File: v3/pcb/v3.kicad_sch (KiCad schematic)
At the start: 193 parts, among them SW1 SW_Push, SW10 SW_Push, SW11 SW_Push, SW12 SW_Push, SW13 SW_Push, SW14 SW_Push, SW15 SW_Push, SW16 SW_Push, SW17 SW_Push, SW18 SW_Push, SW19 SW_Push, SW2 SW_Push, SW20 SW_Push, SW21 SW_Push, SW22 SW_Push, SW23 SW_Push, SW24 SW_Push, SW25 SW_Push, SW26 SW_Push, SW27 SW_Push, SW28 SW_Push, SW29 SW_Push, SW3 SW_Push, SW30 SW_Push, SW31 SW_Push, SW32 SW_Push, SW33 SW_Push, SW34 SW_Push, SW35 SW_Push, SW36 SW_Push, SW37 SW_Push, SW38 SW_Push, SW39 SW_Push, SW4 SW_Push, SW40 SW_Push, SW41 SW_Push, SW42 SW_Push, SW43 SW_Push, SW44 SW_Push, SW45 SW_Push, SW46 SW_Push, SW47 SW_Push, SW48 SW_Push, SW49 SW_Push, SW5 SW_Push, SW50 SW_Push, SW51 SW_Push, SW52 SW_Push, SW53 SW_Push, SW54 SW_Push, SW55 SW_Push, SW56 SW_Push, SW57 SW_Push, SW58 SW_Push, SW59 SW_Push, SW6 SW_Push, SW60 SW_Push, SW61 SW_Push, SW62 SW_Push, SW63 SW_Push, SW64 SW_Push, SW65 SW_Push, SW66 SW_Push, SW67 SW_Push, SW68 SW_Push, SW69 SW_Push, SW7 SW_Push, SW70 SW_Push, SW71 SW_Push, SW72 SW_Push, SW73 SW_Push, SW74 SW_Push, SW75 SW_Push, SW76 SW_Push, SW77 SW_Push, SW78 SW_Push, SW79 SW_Push, SW8 SW_Push, SW80 SW_Push, SW81 SW_Push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

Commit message: Add new layout for v3
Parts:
- added D80, D90, D92: D, Diode_SMD:D_SOD-323F, symbol Device:D
- added SW80, SW90, SW92: SW_Push, Switch_Keyboard_Cherry_MX:SW_Cherry_MX_PCB_1.00u, symbol Switch:SW_Push
- renumbered D80 to D81, D81 to D82, D82 to D83, D83 to D84, D84 to D85, D85 to D86, D86 to D87, D87 to D88, D88 to D89, D89 to D91, D90 to D93, D91 to D94, D92 to D95, D93 to D96, D94 to D97, D95 to D98, D96 to D99, SW80 to SW81, SW81 to SW82, SW82 to SW83, SW83 to SW84, SW84 to SW85, SW85 to SW86, SW86 to SW87, SW87 to SW88, SW88 to SW89, SW89 to SW91, SW90 to SW93, SW91 to SW94, SW92 to SW95, SW93 to SW96, SW94 to SW97, SW95 to SW98, SW96 to SW99
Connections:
- net COL12: now also SW80.1
- net COL4: now also SW90.1
- net COL8: now also SW92.1
- net ROW4: now also D80.1 (K)
- net ROW5: now also D90.1 (K), D92.1 (K)
- new net: D80.2 (A), SW80.2
- new net: D90.2 (A), SW90.2
- new net: D92.2 (A), SW92.2

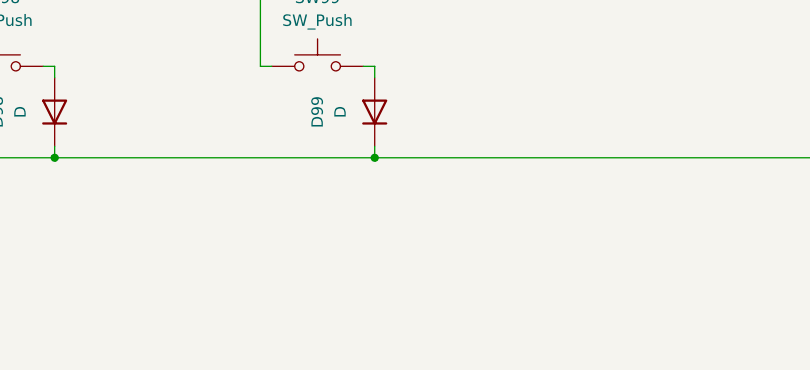
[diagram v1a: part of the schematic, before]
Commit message: Replace switch footprints with hotswap sockets
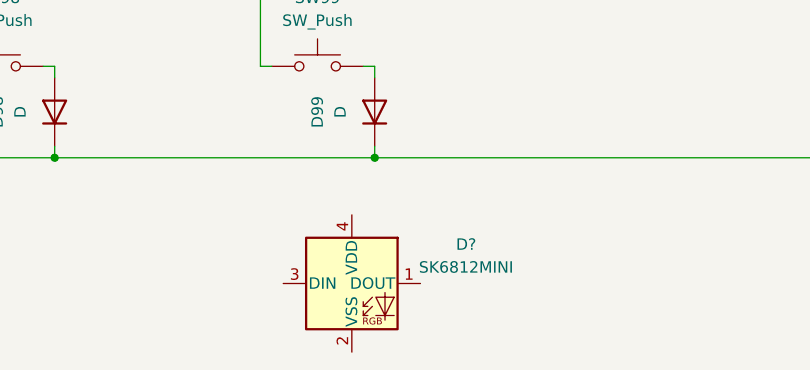
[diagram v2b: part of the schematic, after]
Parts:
- added D?: SK6812MINI, prettylib:SK6812_mini_e_flipable, symbol LED:SK6812MINI
- SW1, SW10, SW11, SW12, SW13, SW14, SW15, SW16, SW17, SW18, SW19, SW2, SW20, SW21, SW22, SW23, SW24, SW25, SW26, SW27, SW28, SW29, SW3, SW30, SW31, SW32, SW33, SW34, SW35, SW36, SW37, SW38, SW39, SW4, SW40, SW41, SW42, SW43, SW44, SW45, SW46, SW47, SW48, SW49, SW5, SW50, SW51, SW52, SW53, SW54, SW55, SW56, SW57, SW58, SW59, SW6, SW60, SW61, SW62, SW63, SW64, SW65, SW66, SW67, SW68, SW69, SW7, SW70, SW71, SW72, SW73, SW74, SW75, SW76, SW77, SW78, SW79, SW8, SW80, SW81, SW82, SW83, SW84, SW85, SW86, SW87, SW88, SW89, SW9, SW90, SW91, SW92, SW93, SW94, SW95, SW96, SW97, SW98, SW99: footprint Switch_Keyboard_Cherry_MX:SW_Cherry_MX_PCB_1.00u -> prettylib:MX_KAILH_SOCKET_1U

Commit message: Add level shifter and everything else for the RGBs
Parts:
- removed D?: SK6812MINI, prettylib:SK6812_mini_e_flipable, symbol LED:SK6812MINI
- added C1, C10, C11, C12, C13, C14, C15, C16, C17, C18, C19, C2, C20, C21, C22, C23, C24, C25, C26, C27, C28, C29, C3, C30, C31, C32, C33, C34, C35, C36, C37, C38, C39, C4, C40, C41, C42, C43, C44, C45, C46, C47, C48, C49, C5, C50, C51, C52, C53, C54, C55, C56, C57, C58, C59, C6, C60, C61, C62, C63, C64, C65, C66, C67, C68, C69, C7, C70, C71, C72, C73, C74, C75, C76, C77, C78, C79, C8, C80, C81, C82, C83, C84, C85, C86, C87, C88, C89, C9, C90, C91, C92, C93, C94, C95, C96, C97, C98, C99: 100n, prettylib:SMD-0603, symbol YAEMK:C
- added RGB1, RGB10, RGB11, RGB12, RGB13, RGB14, RGB15, RGB16, RGB17, RGB18, RGB19, RGB2, RGB20, RGB21, RGB22, RGB23, RGB24, RGB25, RGB27, RGB28, RGB3, RGB30, RGB31, RGB32, RGB33, RGB34, RGB35, RGB36, RGB37, RGB38, RGB39, RGB4, RGB40, RGB41, RGB42, RGB43, RGB44, RGB45, RGB47, RGB48, RGB5, RGB50, RGB51, RGB52, RGB53, RGB54, RGB55, RGB56, RGB57, RGB58, RGB59, RGB60, RGB61, RGB62, RGB63, RGB64, RGB65, RGB67, RGB68, RGB7, RGB70, RGB71, RGB72, RGB73, RGB74, RGB75, RGB76, RGB77, RGB78, RGB79, RGB8, RGB80, RGB81, RGB82, RGB83, RGB84, RGB85, RGB87, RGB88, RGB90, RGB91, RGB92, RGB93, RGB94, RGB95, RGB96, RGB97, RGB98, RGB99: SK6812Mini-e, prettylib:SK6812_mini_e_flipable, symbol YAEMK:SK6812MINI-E
- added RGB26, RGB29, RGB46, RGB49, RGB6, RGB66, RGB69, RGB86, RGB89, RGB9: SK6812Mini, prettylib:SK6812_mini_e_flipable, symbol YAEMK:SK6812MINI
- added TP1: Joystick X, TestPoint:TestPoint_THTPad_D1.5mm_Drill0.7mm, symbol Connector:TestPoint
- added TP2: Joystick VDD, TestPoint:TestPoint_THTPad_D1.5mm_Drill0.7mm, symbol Connector:TestPoint
- added TP3: Joystick Y, TestPoint:TestPoint_THTPad_D1.5mm_Drill0.7mm, symbol Connector:TestPoint
- added TP4: Joystick GND, TestPoint:TestPoint_THTPad_D1.5mm_Drill0.7mm, symbol Connector:TestPoint
- added U2: SN74LVC1T45DCK, Package_TO_SOT_SMD:SOT-363_SC-70-6, symbol Logic_LevelTranslator:SN74LVC1T45DCK
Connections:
- net COL0: now also U1.32 (35_A16_PWM); no longer U1.2 (0_RX1_MOSI1_Touch)
- net COL1: now also D1.1 (K), D10.1 (K), D11.1 (K), D12.1 (K), D13.1 (K), D2.1 (K), D3.1 (K), D4.1 (K), D5.1 (K), D6.1 (K), D7.1 (K), D8.1 (K), D9.1 (K), U1.31 (34_A15_RX5_CAN1RX_SDA0), U1.7 (5_PWM_TX1_MISO1); no longer SW15.1, SW34.1, SW53.1, SW88.1, U1.3 (1_TX1_MISO1_Touch)
- net COL10: now also U1.17 (25); no longer U1.12 (10_PWM_TX2_CS0)
- net COL11: now also U1.16 (24); no longer U1.13 (11_MOSI0)
- net COL13: now also U1.13 (11_MOSI0); no longer U1.16 (24)
- net COL14: now also U1.12 (10_PWM_TX2_CS0); no longer U1.17 (25)
- net COL15: now also U1.11 (9_PWM_RX2_CS0); no longer U1.18 (26_TX1_SCL2)
- net COL16: now also U1.10 (8_TX3_MISO0_SDA0); no longer U1.19 (27_RX1_SCK0)
- net COL17: now also U1.9 (7_RX3_MOSI0_SCL0); no longer U1.20 (28_MOSI0)
- net COL18: now also U1.8 (6_PWM); no longer U1.21 (29_PWM_CAN0TX_Touch)
- net COL2: now also U1.30 (33_A14_TX5_CAN1TX_SCL0); no longer U1.4 (2_PWM)
- net COL3: now also U1.24 (32_A13_TX4_SCK1); no longer U1.5 (3_PWM_CAN0TX_SCL2)
- net COL4: now also U1.23 (31_A12_RX4_CS1); no longer U1.6 (4_PWM_CAN0RX_SDA2)
- net COL5: now also U1.22 (30_PWM_CAN0RX_Touch); no longer U1.7 (5_PWM_TX1_MISO1)
- net COL6: now also U1.21 (29_PWM_CAN0TX_Touch); no longer U1.8 (6_PWM)
- net COL7: now also U1.20 (28_MOSI0); no longer U1.9 (7_RX3_MOSI0_SCL0)
- net COL8: now also U1.19 (27_RX1_SCK0); no longer U1.10 (8_TX3_MISO0_SDA0)
- net COL9: now also U1.18 (26_TX1_SCL2); no longer U1.11 (9_PWM_RX2_CS0)
- net ROW1: now also U1.6 (4_PWM_CAN0RX_SDA2); no longer U1.23 (31_A12_RX4_CS1)
- net ROW2: now also U1.5 (3_PWM_CAN0TX_SCL2); no longer U1.24 (32_A13_TX4_SCK1)
- net ROW3: now also U1.4 (2_PWM); no longer U1.30 (33_A14_TX5_CAN1TX_SCL0)
- net ROW4: now also U1.3 (1_TX1_MISO1_Touch); no longer U1.31 (34_A15_RX5_CAN1RX_SDA0)
- net ROW5: now also U1.2 (0_RX1_MOSI1_Touch); no longer U1.32 (35_A16_PWM)
- net GND: now reaches U1.1 (GND)
- net GND: now also C1.2, C10.2, C11.2, C12.2, C13.2, C14.2, C15.2, C16.2, C17.2, C18.2, C19.2, C2.2, C20.2, C21.2, C22.2, C23.2, C24.2, C25.2, C26.2, C27.2, C28.2, C29.2, C3.2, C30.2, C31.2, C32.2, C33.2, C34.2, C35.2, C36.2, C37.2, C38.2, C39.2, C4.2, C40.2, C41.2, C42.2, C43.2, C44.2, C45.2, C46.2, C47.2, C48.2, C49.2, C5.2, C50.2, C51.2, C52.2, C53.2, C54.2, C55.2, C56.2, C57.2, C58.2, C59.2, C6.2, C60.2, C61.2, C62.2, C63.2, C64.2, C65.2, C66.2, C67.2, C68.2, C69.2, C7.2, C70.2, C71.2, C72.2, C73.2, C74.2, C75.2, C76.2, C77.2, C78.2, C79.2, C8.2, C80.2, C81.2, C82.2, C83.2, C84.2, C85.2, C86.2, C87.2, C88.2, C89.2, C9.2, C90.2, C91.2, C92.2, C93.2, C94.2, C95.2, C96.2, C97.2, C98.2, C99.2, RGB1.3 (VSS), RGB10.3 (VSS), RGB11.3 (VSS), RGB12.3 (VSS), RGB13.3 (VSS), RGB14.3 (VSS), RGB15.3 (VSS), RGB16.3 (VSS), RGB17.3 (VSS), RGB18.3 (VSS), RGB19.3 (VSS), RGB2.3 (VSS), RGB20.3 (VSS), RGB21.3 (VSS), RGB22.3 (VSS), RGB23.3 (VSS), RGB24.3 (VSS), RGB25.3 (VSS), RGB26.2 (VSS), RGB27.3 (VSS), RGB28.3 (VSS), RGB29.2 (VSS), RGB3.3 (VSS), RGB30.3 (VSS), RGB31.3 (VSS), RGB32.3 (VSS), RGB33.3 (VSS), RGB34.3 (VSS), RGB35.3 (VSS), RGB36.3 (VSS), RGB37.3 (VSS), RGB38.3 (VSS), RGB39.3 (VSS), RGB4.3 (VSS), RGB40.3 (VSS), RGB41.3 (VSS), RGB42.3 (VSS), RGB43.3 (VSS), RGB44.3 (VSS), RGB45.3 (VSS), RGB46.2 (VSS), RGB47.3 (VSS), RGB48.3 (VSS), RGB49.2 (VSS), RGB5.3 (VSS), RGB50.3 (VSS), RGB51.3 (VSS), RGB52.3 (VSS), RGB53.3 (VSS), RGB54.3 (VSS), RGB55.3 (VSS), RGB56.3 (VSS), RGB57.3 (VSS), RGB58.3 (VSS), RGB59.3 (VSS), RGB6.2 (VSS), RGB60.3 (VSS), RGB61.3 (VSS), RGB62.3 (VSS), RGB63.3 (VSS), RGB64.3 (VSS), RGB65.3 (VSS), RGB66.2 (VSS), RGB67.3 (VSS), RGB68.3 (VSS), RGB69.2 (VSS), RGB7.3 (VSS), RGB70.3 (VSS), RGB71.3 (VSS), RGB72.3 (VSS), RGB73.3 (VSS), RGB74.3 (VSS), RGB75.3 (VSS), RGB76.3 (VSS), RGB77.3 (VSS), RGB78.3 (VSS), RGB79.3 (VSS), RGB8.3 (VSS), RGB80.3 (VSS), RGB81.3 (VSS), RGB82.3 (VSS), RGB83.3 (VSS), RGB84.3 (VSS), RGB85.3 (VSS), RGB86.2 (VSS), RGB87.3 (VSS), RGB88.3 (VSS), RGB89.2 (VSS), RGB9.2 (VSS), RGB90.3 (VSS), RGB91.3 (VSS), RGB92.3 (VSS), RGB93.3 (VSS), RGB94.3 (VSS), RGB95.3 (VSS), RGB96.3 (VSS), RGB97.3 (VSS), RGB98.3 (VSS), RGB99.3 (VSS), TP4.1, U2.2 (GND), U2.5 (DIR)
- net 3V3REF: now reaches U1.15 (3.3V)
- net 3V3REF: now also U2.6 (VCCB)
- net JOYSTICK_X: now reaches U1.33 (36_A17_PWM)
- net JOYSTICK_X: now also TP1.1
- net JOYSTICK_Y: now reaches U1.34 (37_A18_PWM_SCL1)
- net JOYSTICK_Y: now also TP3.1
- net RGB_3V3_DATA: now reaches U1.35 (38_A19_PWM_SDA1)
- net RGB_3V3_DATA: now also U2.4 (B)
- net VUSB: now reaches U1.54 (VUSB)
- net VUSB: now also U2.1 (VCCA)
- removed net ROW0: D1.1 (K), D10.1 (K), D11.1 (K), D12.1 (K), D13.1 (K), D2.1 (K), D3.1 (K), D4.1 (K), D5.1 (K), D6.1 (K), D7.1 (K), D8.1 (K), D9.1 (K), U1.22 (30_PWM_CAN0RX_Touch)
- new net: RGB65.2 (DOUT), RGB66.3 (DIN)
- new net: RGB64.2 (DOUT), RGB65.4 (DIN)
- new net: RGB31.2 (DOUT), RGB32.4 (DIN)
- new net: RGB30.2 (DOUT), RGB31.4 (DIN)
- new net: RGB45.2 (DOUT), RGB46.3 (DIN)
- new net: RGB44.2 (DOUT), RGB45.4 (DIN)
- new net: SW15.1, SW34.1, SW53.1, SW88.1
- new net: RGB37.2 (DOUT), RGB38.4 (DIN)
- new net: RGB36.2 (DOUT), RGB37.4 (DIN)
- new net: RGB34.2 (DOUT), RGB35.4 (DIN)
- new net: RGB33.2 (DOUT), RGB34.4 (DIN)
- new net: RGB20.2 (DOUT), RGB21.4 (DIN)
- new net: RGB19.2 (DOUT), RGB20.4 (DIN)
- new net: RGB13.2 (DOUT), RGB14.4 (DIN)
- new net: RGB12.2 (DOUT), RGB13.4 (DIN)
- new net: RGB93.2 (DOUT), RGB94.4 (DIN)
- new net: RGB92.2 (DOUT), RGB93.4 (DIN)
- new net: RGB6.1 (DOUT), RGB7.4 (DIN)
- new net: RGB5.2 (DOUT), RGB6.3 (DIN)
- new net: RGB1.2 (DOUT), RGB2.4 (DIN)
- new net: RGB83.2 (DOUT), RGB84.4 (DIN)
- new net: RGB82.2 (DOUT), RGB83.4 (DIN)
- new net: RGB73.2 (DOUT), RGB74.4 (DIN)
- new net: RGB72.2 (DOUT), RGB73.4 (DIN)
- new net: RGB41.2 (DOUT), RGB42.4 (DIN)
- new net: RGB40.2 (DOUT), RGB41.4 (DIN)
- new net: RGB71.2 (DOUT), RGB72.4 (DIN)
- new net: RGB70.2 (DOUT), RGB71.4 (DIN)
- new net: RGB91.2 (DOUT), RGB92.4 (DIN)
- new net: RGB90.2 (DOUT), RGB91.4 (DIN)
- new net: RGB80.2 (DOUT), RGB81.4 (DIN)
- new net: RGB79.2 (DOUT), RGB80.4 (DIN)
- new net: RGB69.1 (DOUT), RGB70.4 (DIN)
- new net: RGB96.2 (DOUT), RGB97.4 (DIN)
- new net: RGB95.2 (DOUT), RGB96.4 (DIN)
- new net: RGB63.2 (DOUT), RGB64.4 (DIN)
- new net: RGB62.2 (DOUT), RGB63.4 (DIN)
- new net: RGB8.2 (DOUT), RGB9.3 (DIN)
- new net: RGB7.2 (DOUT), RGB8.4 (DIN)
- new net: RGB43.2 (DOUT), RGB44.4 (DIN)
- new net: RGB42.2 (DOUT), RGB43.4 (DIN)
- new net: RGB2.2 (DOUT), RGB3.4 (DIN)
- new net: RGB61.2 (DOUT), RGB62.4 (DIN)
- new net: RGB94.2 (DOUT), RGB95.4 (DIN)
- new net: RGB81.2 (DOUT), RGB82.4 (DIN)
- new net: RGB22.2 (DOUT), RGB23.4 (DIN)
- new net: RGB21.2 (DOUT), RGB22.4 (DIN)
- new net: RGB77.2 (DOUT), RGB78.4 (DIN)
- new net: RGB76.2 (DOUT), RGB77.4 (DIN)
- new net: RGB47.2 (DOUT), RGB48.4 (DIN)
- new net: RGB46.1 (DOUT), RGB47.4 (DIN)
- new net: RGB67.2 (DOUT), RGB68.4 (DIN)
- new net: RGB66.1 (DOUT), RGB67.4 (DIN)
- new net: RGB50.2 (DOUT), RGB51.4 (DIN)
- new net: RGB49.1 (DOUT), RGB50.4 (DIN)
- new net: RGB11.2 (DOUT), RGB12.4 (DIN)
- new net: RGB58.2 (DOUT), RGB59.4 (DIN)
- new net: RGB57.2 (DOUT), RGB58.4 (DIN)
- new net: RGB15.2 (DOUT), RGB16.4 (DIN)
- new net: RGB14.2 (DOUT), RGB15.4 (DIN)
- new net: RGB55.2 (DOUT), RGB56.4 (DIN)
- new net: RGB54.2 (DOUT), RGB55.4 (DIN)
- new net: RGB51.2 (DOUT), RGB52.4 (DIN)
- new net: RGB32.2 (DOUT), RGB33.4 (DIN)
- new net: RGB52.2 (DOUT), RGB53.4 (DIN)
- new net: RGB35.2 (DOUT), RGB36.4 (DIN)
- new net: RGB10.2 (DOUT), RGB11.4 (DIN)
- new net: RGB10.4 (DIN), RGB9.1 (DOUT)
- new net: RGB60.2 (DOUT), RGB61.4 (DIN)
- new net: RGB48.2 (DOUT), RGB49.3 (DIN)
- new net: RGB98.2 (DOUT), RGB99.4 (DIN)
- new net: RGB28.2 (DOUT), RGB29.3 (DIN)
- new net: RGB27.2 (DOUT), RGB28.4 (DIN)
- new net: RGB59.2 (DOUT), RGB60.4 (DIN)
- new net: RGB26.1 (DOUT), RGB27.4 (DIN)
- new net: RGB87.2 (DOUT), RGB88.4 (DIN)
- new net: RGB86.1 (DOUT), RGB87.4 (DIN)
- new net: RGB24.2 (DOUT), RGB25.4 (DIN)
- new net: RGB23.2 (DOUT), RGB24.4 (DIN)
- new net: RGB29.1 (DOUT), RGB30.4 (DIN)
- new net: RGB3.2 (DOUT), RGB4.4 (DIN)
- new net: RGB56.2 (DOUT), RGB57.4 (DIN)
- new net: RGB75.2 (DOUT), RGB76.4 (DIN)
- new net: RGB74.2 (DOUT), RGB75.4 (DIN)
- new net: RGB18.2 (DOUT), RGB19.4 (DIN)
- new net: RGB84.2 (DOUT), RGB85.4 (DIN)
- new net: RGB89.1 (DOUT), RGB90.4 (DIN)
- new net: RGB17.2 (DOUT), RGB18.4 (DIN)
- new net: RGB16.2 (DOUT), RGB17.4 (DIN)
- new net: RGB39.2 (DOUT), RGB40.4 (DIN)
- new net: RGB68.2 (DOUT), RGB69.3 (DIN)
- new net: RGB53.2 (DOUT), RGB54.4 (DIN)
- new net: RGB85.2 (DOUT), RGB86.3 (DIN)
- new net: RGB4.2 (DOUT), RGB5.4 (DIN)
- new net: RGB97.2 (DOUT), RGB98.4 (DIN)
- new net: RGB38.2 (DOUT), RGB39.4 (DIN)
- new net: RGB78.2 (DOUT), RGB79.4 (DIN)
- new net: RGB88.2 (DOUT), RGB89.3 (DIN)
- new net: RGB25.2 (DOUT), RGB26.3 (DIN)
- new net RGB_DATA: RGB1.4 (DIN), U2.3 (A)
- new net RGB_VDD: C1.1, C10.1, C11.1, C12.1, C13.1, C14.1, C15.1, C16.1, C17.1, C18.1, C19.1, C2.1, C20.1, C21.1, C22.1, C23.1, C24.1, C25.1, C26.1, C27.1, C28.1, C29.1, C3.1, C30.1, C31.1, C32.1, C33.1, C34.1, C35.1, C36.1, C37.1, C38.1, C39.1, C4.1, C40.1, C41.1, C42.1, C43.1, C44.1, C45.1, C46.1, C47.1, C48.1, C49.1, C5.1, C50.1, C51.1, C52.1, C53.1, C54.1, C55.1, C56.1, C57.1, C58.1, C59.1, C6.1, C60.1, C61.1, C62.1, C63.1, C64.1, C65.1, C66.1, C67.1, C68.1, C69.1, C7.1, C70.1, C71.1, C72.1, C73.1, C74.1, C75.1, C76.1, C77.1, C78.1, C79.1, C8.1, C80.1, C81.1, C82.1, C83.1, C84.1, C85.1, C86.1, C87.1, C88.1, C89.1, C9.1, C90.1, C91.1, C92.1, C93.1, C94.1, C95.1, C96.1, C97.1, C98.1, C99.1, RGB1.1 (VDD), RGB10.1 (VDD), RGB11.1 (VDD), RGB12.1 (VDD), RGB13.1 (VDD), RGB14.1 (VDD), RGB15.1 (VDD), RGB16.1 (VDD), RGB17.1 (VDD), RGB18.1 (VDD), RGB19.1 (VDD), RGB2.1 (VDD), RGB20.1 (VDD), RGB21.1 (VDD), RGB22.1 (VDD), RGB23.1 (VDD), RGB24.1 (VDD), RGB25.1 (VDD), RGB26.4 (VDD), RGB27.1 (VDD), RGB28.1 (VDD), RGB29.4 (VDD), RGB3.1 (VDD), RGB30.1 (VDD), RGB31.1 (VDD), RGB32.1 (VDD), RGB33.1 (VDD), RGB34.1 (VDD), RGB35.1 (VDD), RGB36.1 (VDD), RGB37.1 (VDD), RGB38.1 (VDD), RGB39.1 (VDD), RGB4.1 (VDD), RGB40.1 (VDD), RGB41.1 (VDD), RGB42.1 (VDD), RGB43.1 (VDD), RGB44.1 (VDD), RGB45.1 (VDD), RGB46.4 (VDD), RGB47.1 (VDD), RGB48.1 (VDD), RGB49.4 (VDD), RGB5.1 (VDD), RGB50.1 (VDD), RGB51.1 (VDD), RGB52.1 (VDD), RGB53.1 (VDD), RGB54.1 (VDD), RGB55.1 (VDD), RGB56.1 (VDD), RGB57.1 (VDD), RGB58.1 (VDD), RGB59.1 (VDD), RGB6.4 (VDD), RGB60.1 (VDD), RGB61.1 (VDD), RGB62.1 (VDD), RGB63.1 (VDD), RGB64.1 (VDD), RGB65.1 (VDD), RGB66.4 (VDD), RGB67.1 (VDD), RGB68.1 (VDD), RGB69.4 (VDD), RGB7.1 (VDD), RGB70.1 (VDD), RGB71.1 (VDD), RGB72.1 (VDD), RGB73.1 (VDD), RGB74.1 (VDD), RGB75.1 (VDD), RGB76.1 (VDD), RGB77.1 (VDD), RGB78.1 (VDD), RGB79.1 (VDD), RGB8.1 (VDD), RGB80.1 (VDD), RGB81.1 (VDD), RGB82.1 (VDD), RGB83.1 (VDD), RGB84.1 (VDD), RGB85.1 (VDD), RGB86.4 (VDD), RGB87.1 (VDD), RGB88.1 (VDD), RGB89.4 (VDD), RGB9.4 (VDD), RGB90.1 (VDD), RGB91.1 (VDD), RGB92.1 (VDD), RGB93.1 (VDD), RGB94.1 (VDD), RGB95.1 (VDD), RGB96.1 (VDD), RGB97.1 (VDD), RGB98.1 (VDD), RGB99.1 (VDD), TP2.1
- no-connect marks 0 -> 6
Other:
- title: (none) -> ZeKeyboard V3
- moved on the sheet: U1

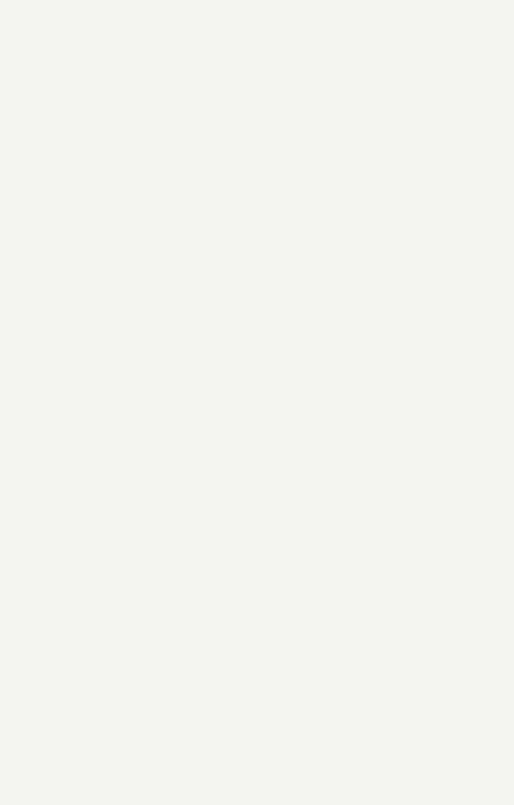
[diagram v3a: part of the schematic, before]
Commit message: Align LED:s and add stabilizer holes
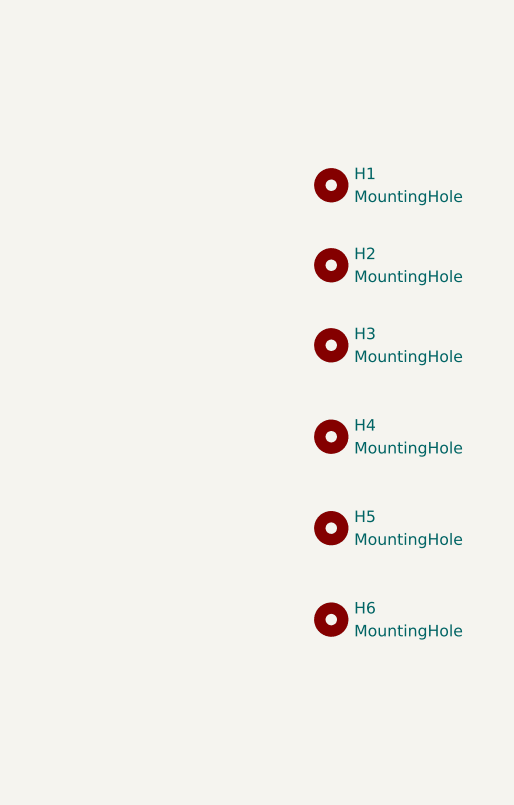
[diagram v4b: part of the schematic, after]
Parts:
- added H1, H2, H3, H4, H5, H6: MountingHole, MountingHole:MountingHole_3.5mm, symbol Mechanical:MountingHole
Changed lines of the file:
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@@
     (pin "2")
   )
+  (symbol (lib_id "Mechanical:MountingHole") (at 734.06 134.62 0) (unit 1)
+    (in_bom yes) (on_board yes) (fields_autoplaced)
+    (property "Reference" "H5" (id 0) (at 736.6 133.3499 0)
+      (effects (font (size 1.27 1.27)) (justify left))
+    )
+    (property "Value" "MountingHole" (id 1) (at 736.6 135.8899 0)
+      (effects (font (size 1.27 1.27)) (justify left))
+    )
+    (property "Footprint" "MountingHole:MountingHole_3.5mm" (id 2) (at 734.06 134.62 0)
+      (effects (font (size 1.27 1.27)) hide)
+    )
+    (property "Datasheet" "~" (id 3) (at 734.06 134.62 0)
+      (effects (font (size 1.27 1.27)) hide)
+    )
+  )
   (symbol (lib_id "Switch:SW_Push") (at 257.81 148.59 0) (unit 1)
     (in_bom yes) (on_board yes) (fields_autoplaced)
@@
     (pin "2")
   )
+  (symbol (lib_id "Mechanical:MountingHole") (at 734.06 114.3 0) (unit 1)
+    (in_bom yes) (on_board yes) (fields_autoplaced)
+    (property "Reference" "H3" (id 0) (at 736.6 113.0299 0)
+      (effects (font (size 1.27 1.27)) (justify left))
+    )
+    (property "Value" "MountingHole" (id 1) (at 736.6 115.5699 0)
+      (effects (font (size 1.27 1.27)) (justify left))
+    )
+    (property "Footprint" "MountingHole:MountingHole_3.5mm" (id 2) (at 734.06 114.3 0)
+      (effects (font (size 1.27 1.27)) hide)
+    )
+    (property "Datasheet" "~" (id 3) (at 734.06 114.3 0)
+      (effects (font (size 1.27 1.27)) hide)
+    )
+  )
   (symbol (lib_id "Device:D") (at 157.48 113.03 90) (unit 1)
     (in_bom yes) (on_board yes)
@@
     (pin "2")
   )
+  (symbol (lib_id "Mechanical:MountingHole") (at 734.06 96.52 0) (unit 1)
+    (in_bom yes) (on_board yes) (fields_autoplaced)
+    (property "Reference" "H1" (id 0) (at 736.6 95.2499 0)
+      (effects (font (size 1.27 1.27)) (justify left))
+    )
+    (property "Value" "MountingHole" (id 1) (at 736.6 97.7899 0)
+      (effects (font (size 1.27 1.27)) (justify left))
+    )
+    (property "Footprint" "MountingHole:MountingHole_3.5mm" (id 2) (at 734.06 96.52 0)
+      (effects (font (size 1.27 1.27)) hide)
+    )
+    (property "Datasheet" "~" (id 3) (at 734.06 96.52 0)
+      (effects (font (size 1.27 1.27)) hide)
+    )
+  )
   (symbol (lib_id "Switch:SW_Push") (at 63.5 87.63 0) (unit 1)
     (in_bom yes) (on_board yes) (fields_autoplaced)
@@
     (pin "4")
   )
+  (symbol (lib_id "Mechanical:MountingHole") (at 734.06 105.41 0) (unit 1)
+    (in_bom yes) (on_board yes) (fields_autoplaced)
+    (property "Reference" "H2" (id 0) (at 736.6 104.1399 0)
+      (effects (font (size 1.27 1.27)) (justify left))
+    )
+    (property "Value" "MountingHole" (id 1) (at 736.6 106.6799 0)
+      (effects (font (size 1.27 1.27)) (justify left))
+    )
+    (property "Footprint" "MountingHole:MountingHole_3.5mm" (id 2) (at 734.06 105.41 0)
+      (effects (font (size 1.27 1.27)) hide)
+    )
+    (property "Datasheet" "~" (id 3) (at 734.06 105.41 0)
+      (effects (font (size 1.27 1.27)) hide)
+    )
+  )
   (symbol (lib_id "Device:D") (at 246.38 173.99 90) (unit 1)
     (in_bom yes) (on_board yes)
@@
     (pin "2")
   )
+  (symbol (lib_id "Mechanical:MountingHole") (at 734.06 124.46 0) (unit 1)
+    (in_bom yes) (on_board yes) (fields_autoplaced)
+    (property "Reference" "H4" (id 0) (at 736.6 123.1899 0)
+      (effects (font (size 1.27 1.27)) (justify left))
+    )
+    (property "Value" "MountingHole" (id 1) (at 736.6 125.7299 0)
+      (effects (font (size 1.27 1.27)) (justify left))
+    )
+    (property "Footprint" "MountingHole:MountingHole_3.5mm" (id 2) (at 734.06 124.46 0)
+      (effects (font (size 1.27 1.27)) hide)
+    )
+    (property "Datasheet" "~" (id 3) (at 734.06 124.46 0)
+      (effects (font (size 1.27 1.27)) hide)
+    )
+  )
   (symbol (lib_id "YAEMK:C") (at 595.63 304.8 0) (unit 1)
     (in_bom yes) (on_board yes)
@@
     (pin "4")
   )
+  (symbol (lib_id "Mechanical:MountingHole") (at 734.06 144.78 0) (unit 1)
+    (in_bom yes) (on_board yes) (fields_autoplaced)
+    (property "Reference" "H6" (id 0) (at 736.6 143.5099 0)
+      (effects (font (size 1.27 1.27)) (justify left))
+    )
+    (property "Value" "MountingHole" (id 1) (at 736.6 146.0499 0)
+      (effects (font (size 1.27 1.27)) (justify left))
+    )
+    (property "Footprint" "MountingHole:MountingHole_3.5mm" (id 2) (at 734.06 144.78 0)
+      (effects (font (size 1.27 1.27)) hide)
+    )
+    (property "Datasheet" "~" (id 3) (at 734.06 144.78 0)
+      (effects (font (size 1.27 1.27)) hide)
+    )
+  )
   (symbol (lib_id "Switch:SW_Push") (at 293.37 128.27 0) (unit 1)
     (in_bom yes) (on_board yes) (fields_autoplaced)
@@
       (reference "D99") (unit 1) (value "D") (footprint "Diode_SMD:D_SOD-323F")
     )
+    (path "/5958b93f-f3f1-4e43-827a-587abe2ea819"
+      (reference "H1") (unit 1) (value "MountingHole") (footprint "MountingHole:MountingHole_3.5mm")
+    )
+    (path "/9c9c82f9-dbdc-4b15-a250-c779c124834f"
+      (reference "H2") (unit 1) (value "MountingHole") (footprint "MountingHole:MountingHole_3.5mm")
+    )
+    (path "/5187d9fa-0638-4a10-a516-0d85172ecf43"
+      (reference "H3") (unit 1) (value "MountingHole") (footprint "MountingHole:MountingHole_3.5mm")
+    )
+    (path "/ab92cc58-61a7-44e9-a7d2-b180b1c173a2"
+      (reference "H4") (unit 1) (value "MountingHole") (footprint "MountingHole:MountingHole_3.5mm")
+    )
+    (path "/0851e5e4-8e9a-4403-ae5c-f92d4e60675b"
+      (reference "H5") (unit 1) (value "MountingHole") (footprint "MountingHole:MountingHole_3.5mm")
+    )
+    (path "/e22cee4b-2200-4623-b07d-7ce80df62a27"
+      (reference "H6") (unit 1) (value "MountingHole") (footprint "MountingHole:MountingHole_3.5mm")
+    )
     (path "/253abb66-0615-40f8-bfb9-4da73109605e"

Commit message: Reorient LEDs and started on USB
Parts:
- removed RGB44, RGB45, RGB47, RGB48, RGB50, RGB51, RGB81, RGB82, RGB83, RGB84, RGB85: SK6812Mini-e, prettylib:SK6812_mini_e_flipable, symbol YAEMK:SK6812MINI-E
- removed RGB46, RGB49, RGB86: SK6812Mini, prettylib:SK6812_mini_e_flipable, symbol YAEMK:SK6812MINI
- added FB?: fb_0402_26ohm, Bonsai_C4:R_0402_1005Metric, symbol Bonsai_C4:fb_0402_26ohm
- added J?: USB_C_Receptacle_USB2.0, Connector_USB:USB_C_Receptacle_HRO_TYPE-C-31-M-12, symbol Connector:USB_C_Receptacle_USB2.0
- added R? (x2): 5.1k, Resistor_SMD:R_0603_1608Metric, symbol keyboard-left-rescue:R-Device-keyboard-right-rescue
- added RGB33, RGB34, RGB35, RGB36, RGB37, RGB38, RGB39, RGB40, RGB69, RGB70, RGB71, RGB72, RGB73, RGB74: SK6812Mini-e, prettylib:SK6812_mini_e_flipable, symbol YAEMK:SK6812MINI-E
- RGB26, RGB29, RGB66, RGB89: value SK6812Mini -> SK6812Mini-e; symbol YAEMK:SK6812MINI -> YAEMK:SK6812MINI-E
- RGB5: renamed from RGB9; value SK6812Mini -> SK6812Mini-e; symbol YAEMK:SK6812MINI -> YAEMK:SK6812MINI-E
- RGB8: renamed from RGB6; value SK6812Mini -> SK6812Mini-e; symbol YAEMK:SK6812MINI -> YAEMK:SK6812MINI-E
- RGB86: renamed from RGB69; value SK6812Mini -> SK6812Mini-e; symbol YAEMK:SK6812MINI -> YAEMK:SK6812MINI-E
- SW27, SW64, SW91, SW92, SW98: footprint prettylib:MX_KAILH_SOCKET_1U -> zekeyboard:MX_KAILH_SOCKET_2U_STAB
- SW51, SW86: footprint prettylib:MX_KAILH_SOCKET_1U -> zekeyboard:MX_KAILH_SOCKET_2U_STAB_VERT
- renumbered RGB13 to RGB1, RGB4 to RGB10, RGB3 to RGB11, RGB2 to RGB12, RGB1 to RGB13, RGB12 to RGB2, RGB11 to RGB3, RGB10 to RGB4, RGB40 to RGB44, RGB39 to RGB45, RGB38 to RGB46, RGB37 to RGB47, RGB36 to RGB48, RGB35 to RGB49, RGB34 to RGB50, RGB33 to RGB51, RGB8 to RGB6, RGB80 to RGB75, RGB79 to RGB76, RGB78 to RGB77, RGB77 to RGB78, RGB76 to RGB79, RGB75 to RGB80, RGB74 to RGB81, RGB73 to RGB82, RGB72 to RGB83, RGB71 to RGB84, RGB70 to RGB85, RGB5 to RGB9
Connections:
- net GND: now also RGB26.3 (VSS), RGB29.3 (VSS), RGB5.3 (VSS), RGB66.3 (VSS), RGB8.3 (VSS), RGB86.3 (VSS), RGB89.3 (VSS), FB?.2, J?.A1 (GND), J?.A12 (GND), J?.B1 (GND), J?.B12 (GND), R?.1, R?.1, RGB33.3 (VSS), RGB34.3 (VSS), RGB35.3 (VSS), RGB36.3 (VSS), RGB37.3 (VSS), RGB38.3 (VSS), RGB39.3 (VSS), RGB40.3 (VSS), RGB69.3 (VSS), RGB70.3 (VSS), RGB71.3 (VSS), RGB72.3 (VSS), RGB73.3 (VSS), RGB74.3 (VSS); no longer RGB26.2 (VSS), RGB29.2 (VSS), RGB5.2 (VSS), RGB66.2 (VSS), RGB8.2 (VSS), RGB86.2 (VSS), RGB89.2 (VSS)
- net RGB_VDD: now also RGB26.1 (VDD), RGB29.1 (VDD), RGB5.1 (VDD), RGB66.1 (VDD), RGB8.1 (VDD), RGB89.1 (VDD), RGB33.1 (VDD), RGB34.1 (VDD), RGB35.1 (VDD), RGB36.1 (VDD), RGB37.1 (VDD), RGB38.1 (VDD), RGB39.1 (VDD), RGB40.1 (VDD); no longer RGB26.4 (VDD), RGB29.4 (VDD), RGB5.4 (VDD), RGB66.4 (VDD), RGB75.1 (VDD), RGB76.1 (VDD), RGB77.1 (VDD), RGB78.1 (VDD), RGB79.1 (VDD), RGB8.4 (VDD), RGB80.1 (VDD), RGB81.1 (VDD), RGB82.1 (VDD), RGB83.1 (VDD), RGB84.1 (VDD), RGB85.1 (VDD), RGB86.4 (VDD), RGB89.4 (VDD)
- net at RGB65.2 (DOUT): now also RGB66.4 (DIN); no longer RGB66.3 (DIN)
- net at RGB7.4 (DIN): now also RGB8.2 (DOUT); no longer RGB8.1 (DOUT)
- net at RGB9.2 (DOUT): now also RGB8.4 (DIN); no longer RGB8.3 (DIN)
- net at RGB42.4 (DIN): now also RGB43.2 (DOUT); no longer RGB41.2 (DOUT)
- net at RGB41.4 (DIN): now also RGB42.2 (DOUT); no longer RGB44.2 (DOUT)
- net at RGB75.2 (DOUT): now also RGB74.4 (DIN)
- net at RGB86.1 (VDD): now also RGB75.1 (VDD), RGB76.1 (VDD), RGB77.1 (VDD), RGB78.1 (VDD), RGB79.1 (VDD), RGB80.1 (VDD), RGB81.1 (VDD), RGB82.1 (VDD), RGB83.1 (VDD), RGB84.1 (VDD), RGB85.1 (VDD), RGB69.1 (VDD), RGB70.1 (VDD), RGB71.1 (VDD), RGB72.1 (VDD), RGB73.1 (VDD), RGB74.1 (VDD); no longer RGB85.4 (DIN)
- net at RGB6.2 (DOUT): now also RGB5.4 (DIN); no longer RGB5.3 (DIN)
- net at RGB43.4 (DIN): now also RGB44.2 (DOUT); no longer RGB42.2 (DOUT)
- net at RGB67.4 (DIN): now also RGB66.2 (DOUT); no longer RGB66.1 (DOUT)
- net at RGB52.4 (DIN): now also RGB33.2 (DOUT)
- net at RGB4.4 (DIN): now also RGB5.2 (DOUT); no longer RGB5.1 (DOUT)
- net at RGB28.2 (DOUT): now also RGB29.4 (DIN); no longer RGB29.3 (DIN)
- net at RGB27.4 (DIN): now also RGB26.2 (DOUT); no longer RGB26.1 (DOUT)
- net at RGB87.4 (DIN): now also RGB69.2 (DOUT)
- net at RGB30.4 (DIN): now also RGB29.2 (DOUT); no longer RGB29.1 (DOUT)
- net at RGB90.4 (DIN): now also RGB89.2 (DOUT); no longer RGB89.1 (DOUT)
- net at RGB68.2 (DOUT): now also RGB86.4 (DIN); no longer RGB86.3 (DIN)
- net at RGB88.2 (DOUT): now also RGB89.4 (DIN); no longer RGB89.3 (DIN)
- net USB_D-: now reaches U1.59 (A26_D-)
- net USB_D-: now also J?.A7 (D-), J?.B7 (D-)
- net USB_D+: now reaches U1.60 (A25_D+)
- net USB_D+: now also J?.A6 (D+), J?.B6 (D+)
- net at RGB25.2 (DOUT): now also RGB26.4 (DIN); no longer RGB26.3 (DIN)
- new net: RGB35.4 (DIN), RGB36.2 (DOUT)
- new net: RGB36.4 (DIN), RGB37.2 (DOUT)
- new net: J?.A5 (CC1), R?.2
- new net: J?.B5 (CC2), R?.2
- new net: RGB69.4 (DIN), RGB70.2 (DOUT)
- new net: RGB70.4 (DIN), RGB71.2 (DOUT)
- new net: RGB85.4 (DIN), RGB86.2 (DOUT)
- new net: RGB71.4 (DIN), RGB72.2 (DOUT)
- new net: RGB37.4 (DIN), RGB38.2 (DOUT)
- new net: RGB38.4 (DIN), RGB39.2 (DOUT)
- new net: RGB39.4 (DIN), RGB40.2 (DOUT)
- new net: RGB34.4 (DIN), RGB35.2 (DOUT)
- new net: RGB33.4 (DIN), RGB34.2 (DOUT)
- new net: RGB40.4 (DIN), RGB41.2 (DOUT)
- new net: RGB73.4 (DIN), RGB74.2 (DOUT)
- new net: FB?.1, J?.S1 (SHIELD)
- new net: RGB72.4 (DIN), RGB73.2 (DOUT)
- new net: J?.A4 (VBUS), J?.A9 (VBUS), J?.B4 (VBUS), J?.B9 (VBUS)
- no-connect marks 6 -> 8
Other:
- moved on the sheet: RGB1, RGB10, RGB11, RGB12, RGB13, RGB14, RGB15, RGB16, RGB17, RGB18, RGB19, RGB2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
